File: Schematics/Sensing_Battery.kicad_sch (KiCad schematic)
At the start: 4 parts

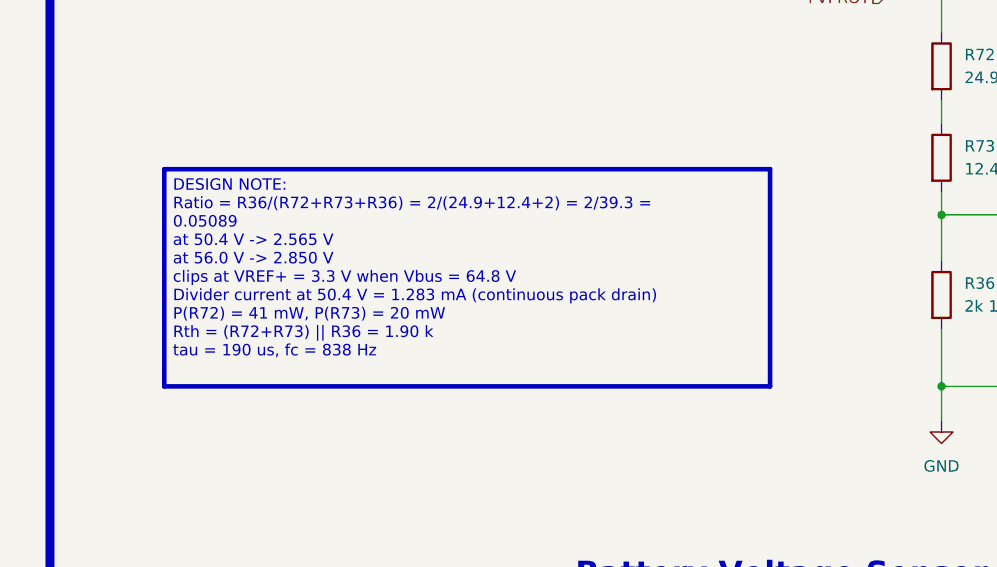
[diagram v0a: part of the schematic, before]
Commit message: Clean up schematic design notes; export schematic and PCB artwork PDFs
- Remove firmware-only notes (boot sequence, calibration procedure,
  firmware SPI/PWM settings) and template/empty text; keep hardware facts
- Tighten wording of all DESIGN/SPEC/ASSEMBLY/REV 1 notes and resize
  boxes so no note text wraps or overflows
- Re-export schematic PDF
- Add PCB artwork PDFs (combined and one per layer: silk, paste, mask,
  L1-L6 copper), board outline on every page

Co-Authored-By: Claude Opus 5.5 <noreply@anthropic.com>
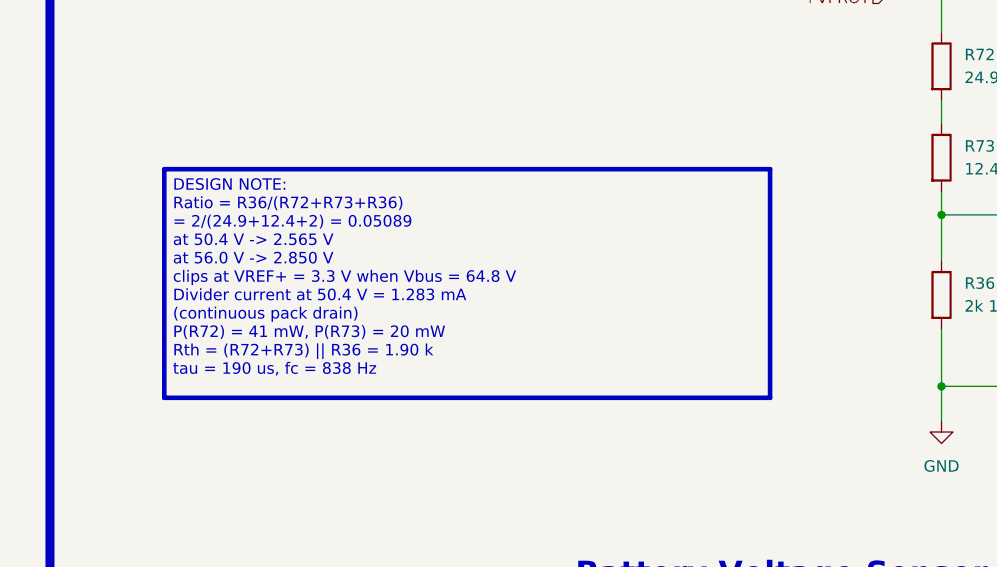
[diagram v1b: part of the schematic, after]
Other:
- company: (none) -> ${COMPANY}
- title: (none) -> Sensing - Battery
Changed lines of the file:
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@@
 	(generator_version "10.0")
 	(paper "A4")
+	(title_block
+		(title "Sensing - Battery")
+		(date "${RELEASE_DATE}")
+		(rev "${REVISION}")
+		(company "${COMPANY}")
+	)
 	(rectangle
 		(start 66.04 54.61)
@@
 		)
 	)
-	(text_box "DESIGN NOTE:\n  Ratio = R36/(R72+R73+R36) = 2/(24.9+12.4+2) = 2/39.3 = 0.05089\n    at 50.4 V -> 2.565 V\n    at 56.0 V -> 2.850 V\n    clips at VREF+ = 3.3 V when Vbus = 64.8 V\n  Divider current at 50.4 V = 1.283 mA (continuous pack drain)\n  P(R72) = 41 mW, P(R73) = 20 mW\n  Rth = (R72+R73) || R36 = 1.90 k\n  tau = 190 us, fc = 838 Hz"
+	(text_box "DESIGN NOTE:\n  Ratio = R36/(R72+R73+R36)\n        = 2/(24.9+12.4+2) = 0.05089\n    at 50.4 V -> 2.565 V\n    at 56.0 V -> 2.850 V\n    clips at VREF+ = 3.3 V when Vbus = 64.8 V\n  Divider current at 50.4 V = 1.283 mA\n    (continuous pack drain)\n  P(R72) = 41 mW, P(R73) = 20 mW\n  Rth = (R72+R73) || R36 = 1.90 k\n  tau = 190 us, fc = 838 Hz"
 		(exclude_from_sim no)
 		(at 78.74 87.63 0)
-		(size 67.31 24.13)
+		(size 67.31 25.40)
 		(margins 0.9525 0.9525 0.9525 0.9525)
 		(stroke
